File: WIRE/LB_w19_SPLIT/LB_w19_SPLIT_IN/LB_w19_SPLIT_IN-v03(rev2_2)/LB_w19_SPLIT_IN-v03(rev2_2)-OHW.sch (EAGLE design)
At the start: 11 parts

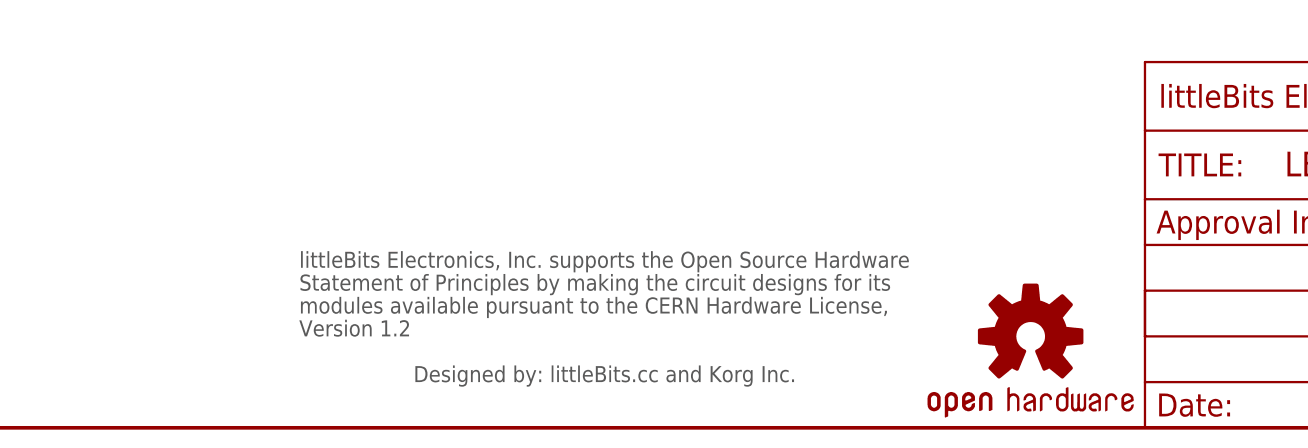
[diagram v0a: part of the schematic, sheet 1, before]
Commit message: Updated license in Korg bits modules
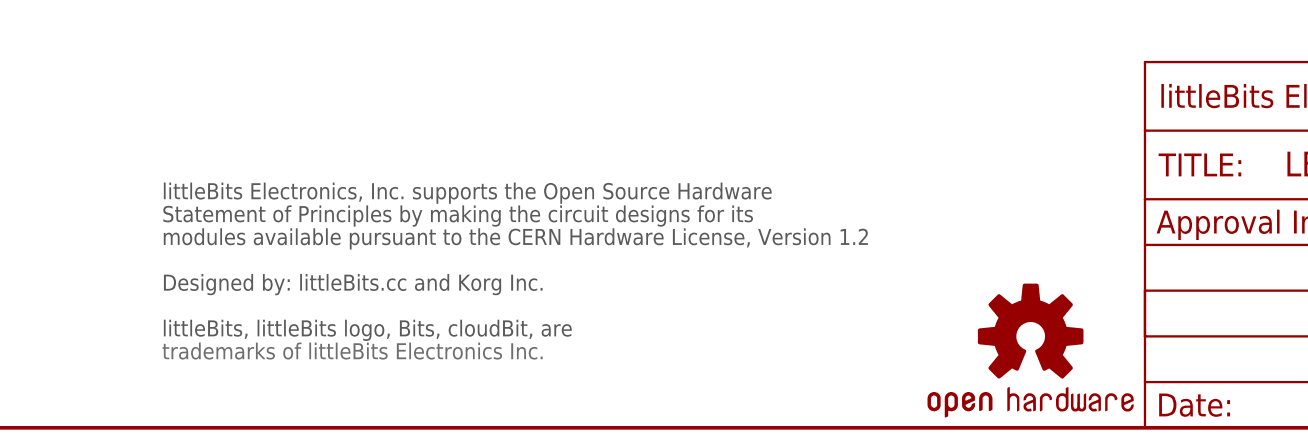
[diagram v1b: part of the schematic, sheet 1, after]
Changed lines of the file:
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@@
 <layer number="111" name="LB_TEXT" color="13" fill="1" visible="yes" active="yes"/>
 <layer number="112" name="tSilk" color="7" fill="1" visible="yes" active="yes"/>
+<layer number="113" name="ReferenceLS" color="7" fill="1" visible="yes" active="yes"/>
 <layer number="116" name="Patch_BOT" color="9" fill="4" visible="yes" active="yes"/>
+<layer number="118" name="Rect_Pads" color="7" fill="1" visible="yes" active="yes"/>
 <layer number="121" name="_tsilk" color="7" fill="1" visible="yes" active="yes"/>
 <layer number="122" name="_bsilk" color="7" fill="1" visible="yes" active="yes"/>
@@
 <instance part="FRAME1" gate="G$1" x="0" y="0"/>
 <instance part="FRAME1" gate="G$2" x="147.32" y="0"/>
-<instance part="U$1" gate="G$1" x="50.8" y="5.08"/>
+<instance part="U$1" gate="G$1" x="35.56" y="12.7"/>
 </instances>
 <busses>
